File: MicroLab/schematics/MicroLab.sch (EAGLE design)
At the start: 100 parts, among them IC1 MC7805CDTG, IC6 LM324D, J1 POWER_JACKPTH, J2 THONKICONN, J3 THONKICONN, Q901 BC846

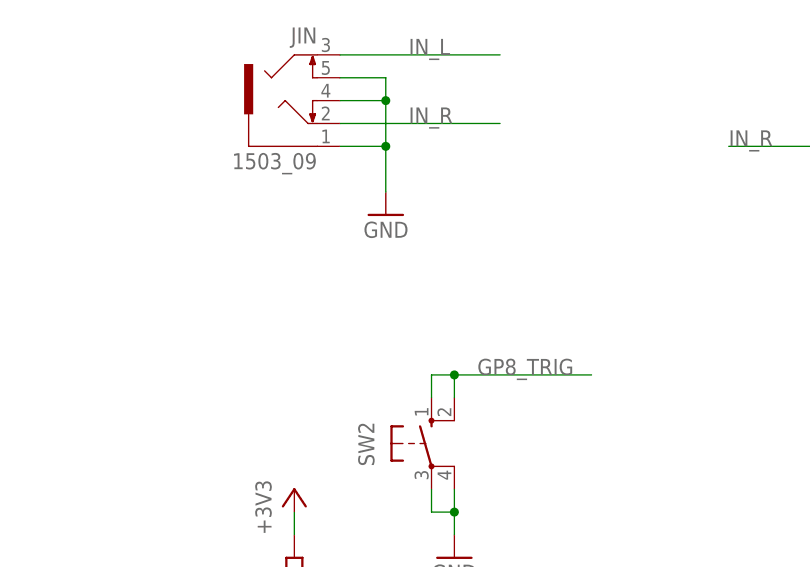
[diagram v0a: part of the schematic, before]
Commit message: added SW3, moved POT_A2
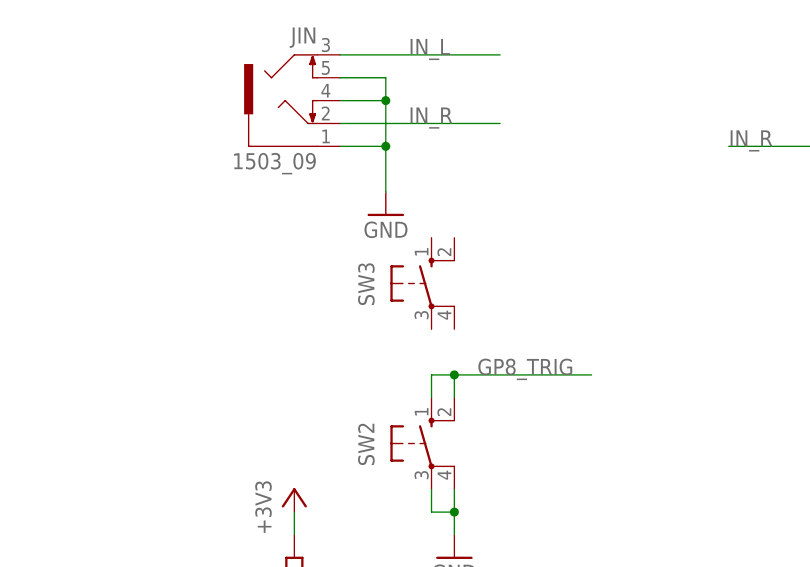
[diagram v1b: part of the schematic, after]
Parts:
- added SW3: (no value), switch-omron:10-XX
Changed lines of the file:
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@@
 <?xml version="1.0" encoding="utf-8"?>
 <!DOCTYPE eagle SYSTEM "eagle.dtd">
-<eagle version="7.5.0">
+<eagle version="7.2.0">
 <drawing>
 <settings>
@@
 <part name="R32" library="Rebel" deviceset="R-EU_" device="0603" value="100R"/>
 <part name="R33" library="Rebel" deviceset="R-EU_" device="0603" value="100R"/>
+<part name="SW3" library="switch-omron" deviceset="10-XX" device=""/>
 </parts>
 <sheets>
@@
 <instance part="R32" gate="G$1" x="231.14" y="157.48" rot="MR180"/>
 <instance part="R33" gate="G$1" x="-53.34" y="48.26" rot="MR180"/>
+<instance part="SW3" gate="1" x="-33.02" y="142.24"/>
 </instances>
 <busses>

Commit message: Completed MicroLab Rev2
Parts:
- removed LED2, LED3, LED4, LED5, LED6, LED7, LED8: KP-3216SGC, SparkFun:LED1206
- removed R15, R23, R24, R25, R27: 1k, Rebel:R-EU_0603
- LED1: value KP-3216SGC -> MULTICOMP_703-1028; device SparkFun:LED1206 -> Rebel:MULTICOMP_703-1028; FARNELL 853-0033 -> (none)
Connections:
- removed net GP9_LEDPWM: R23.1, R25.1, TGP1-4.4
- removed net N$14: LED2.A, R15.2
- removed net N$18: LED7.A, R23.2
- removed net N$20: LED3.A, R24.2
- removed net N$21: LED4.A, R25.2
- removed net N$28: LED5.A, R27.2
- new net GP9_TRIG: SW3.S, SW3.S1, TGP1-4.4
- net +5V: now also LED1.A
- net +9V: now also J1.PWR; no longer J1.GND
- net GND: now also J1.GND, SW3.P, SW3.P1; no longer J1.PWR, LED1.C, LED2.C, LED3.C, LED4.C, LED5.C, LED6.C, LED7.C, LED8.C
- net GP1_LEDPWM: no longer R15.1
- net GP2_LEDPWM: no longer R24.1
- net GP6_LEDPWM: no longer R27.1
- net N$16: now also LED1.CRED; no longer LED1.A
- net N$17: now also LED1.CGREEN; no longer LED6.A
- net N$19: now also LED1.CBLUE; no longer LED8.A
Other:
- moved on the sheet: EXPI, EXPO, J1, J2, JIN, Q901, R21, R22, R28, R33, R34, R36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

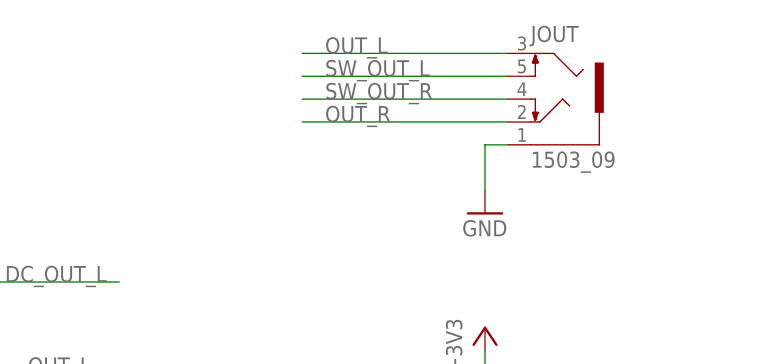
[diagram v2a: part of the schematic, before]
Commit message: removed unused nets from stereo jack
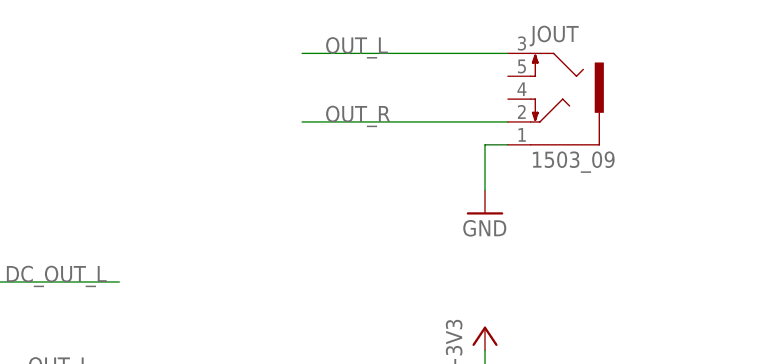
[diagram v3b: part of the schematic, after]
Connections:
- removed net SW_OUT_L: JOUT.5
- removed net SW_OUT_R: JOUT.4
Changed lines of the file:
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@@
-</segment>
-</net>
-<net name="SW_OUT_L" class="0">
-<segment>
-<pinref part="JOUT" gate="G$1" pin="5"/>
-<wire x1="299.72" y1="236.22" x2="276.86" y2="236.22" width="0.1524" layer="91"/>
-<label x="279.4" y="236.22" size="1.778" layer="95"/>
-</segment>
-</net>
-<net name="SW_OUT_R" class="0">
-<segment>
-<pinref part="JOUT" gate="G$1" pin="4"/>
-<wire x1="299.72" y1="233.68" x2="276.86" y2="233.68" width="0.1524" layer="91"/>
-<label x="279.4" y="233.68" size="1.778" layer="95"/>
 </segment>
 </net>

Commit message: MicroLab Rev02
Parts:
- removed POT_A1, POT_A2, POT_A3, POT_A4: POT-ALPS-RK09L1140, Rebel:POT-ALPS-RK09L1140
- added POT_A, POT_B, POT_C, POT_D: POT-ALPS-RK09L1140, Rebel:POT-ALPS-RK09L1140
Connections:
- net +3V3: now also POT_BG$1.3, POT_CG$1.3, POT_DG$1.3; no longer POT_A1G$1.3, POT_A2G$1.3, POT_A4G$1.3
- net ADC1: now also POT_CG$1.2; no longer POT_A1G$1.2
- net ADC2: now also POT_DG$1.2; no longer POT_A2G$1.2
- net ADC3: now also POT_AG$1.2; no longer POT_A3G$1.2
- net ADC4: now also POT_BG$1.2; no longer POT_A4G$1.2
- net GND: now also POT_AG$1.1, POT_AG$2.P$1, POT_BG$1.1, POT_BG$2.P$1, POT_CG$1.1, POT_CG$2.P$1, POT_DG$1.1, POT_DG$2.P$1; no longer POT_A1G$1.1, POT_A1G$2.P$1, POT_A2G$1.1, POT_A2G$2.P$1, POT_A3G$1.1, POT_A3G$2.P$1, POT_A4G$1.1, POT_A4G$2.P$1
- net N$25: now also POT_AG$1.3; no longer POT_A3G$1.3
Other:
- note added: "MicroLab Rev02"
- note removed: "Play Rev01"
- moved on the sheet: D2, J3, JOUT, R29, R30

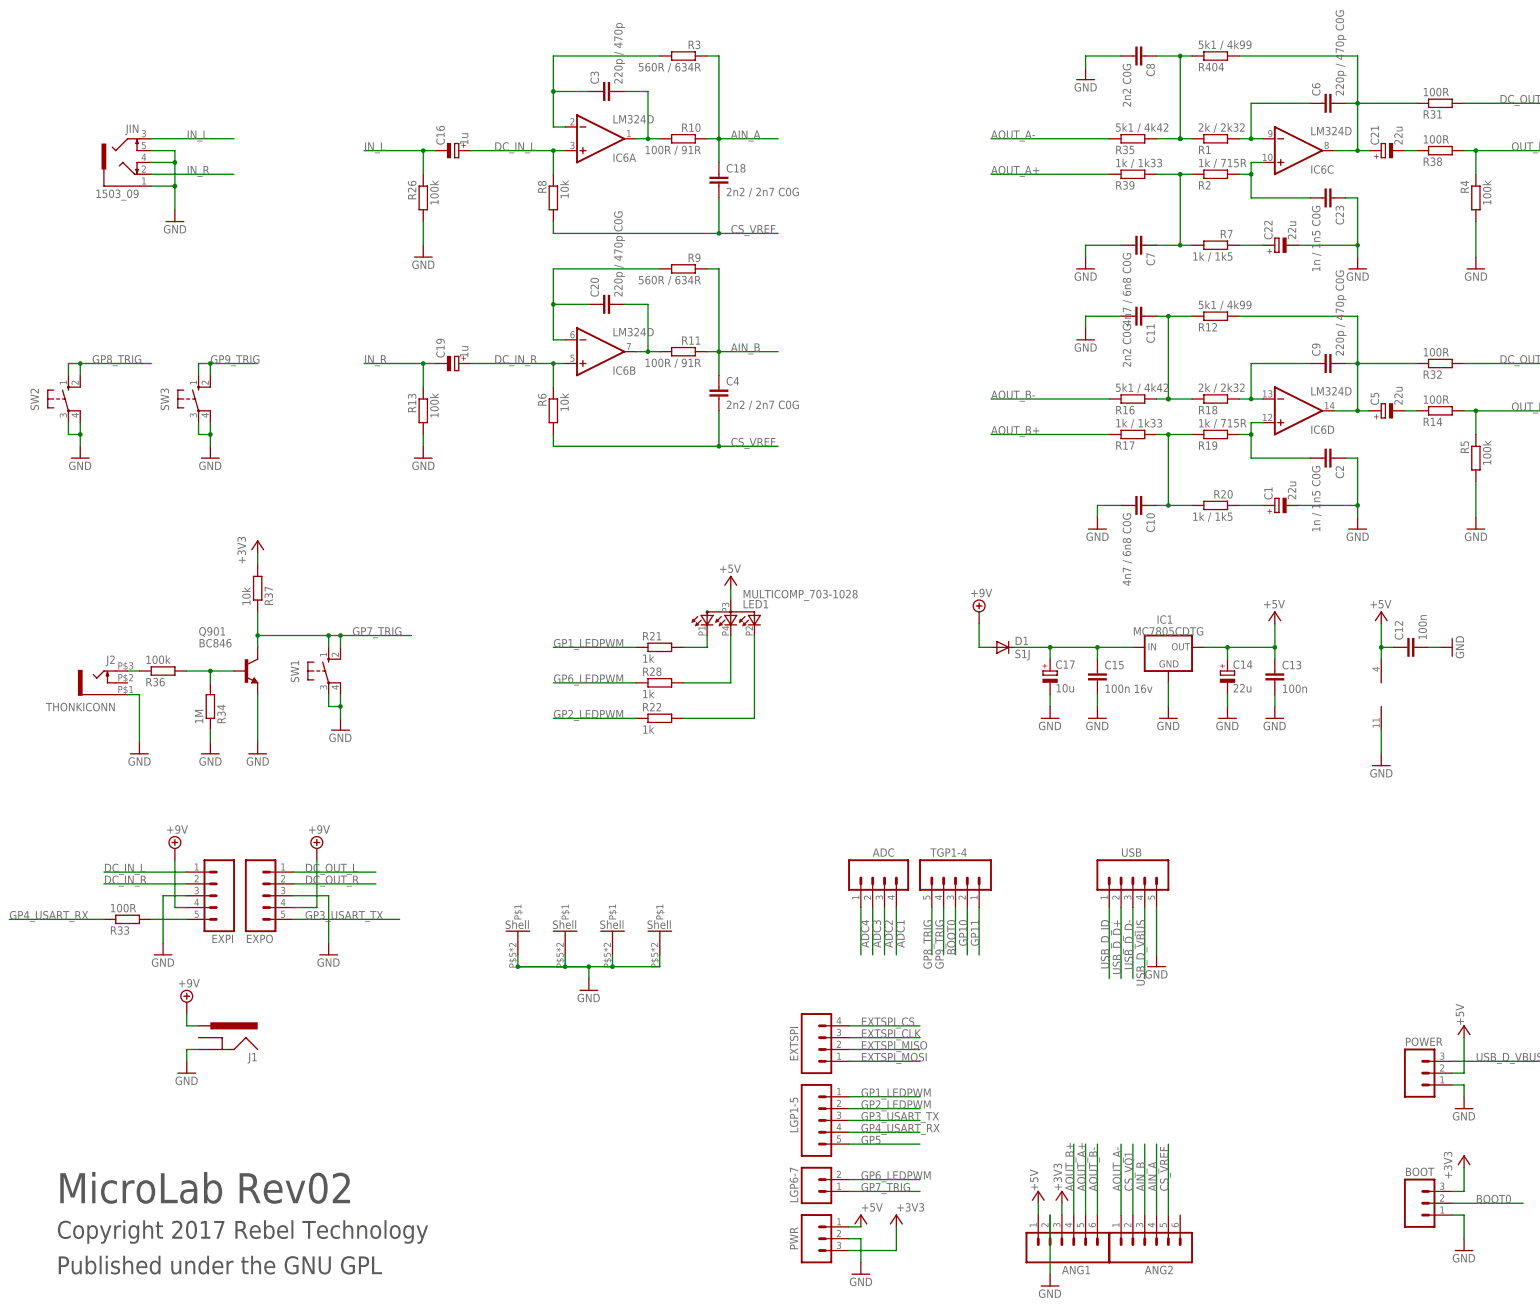
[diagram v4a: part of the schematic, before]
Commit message: changed to JST PH extension headers. Rev03
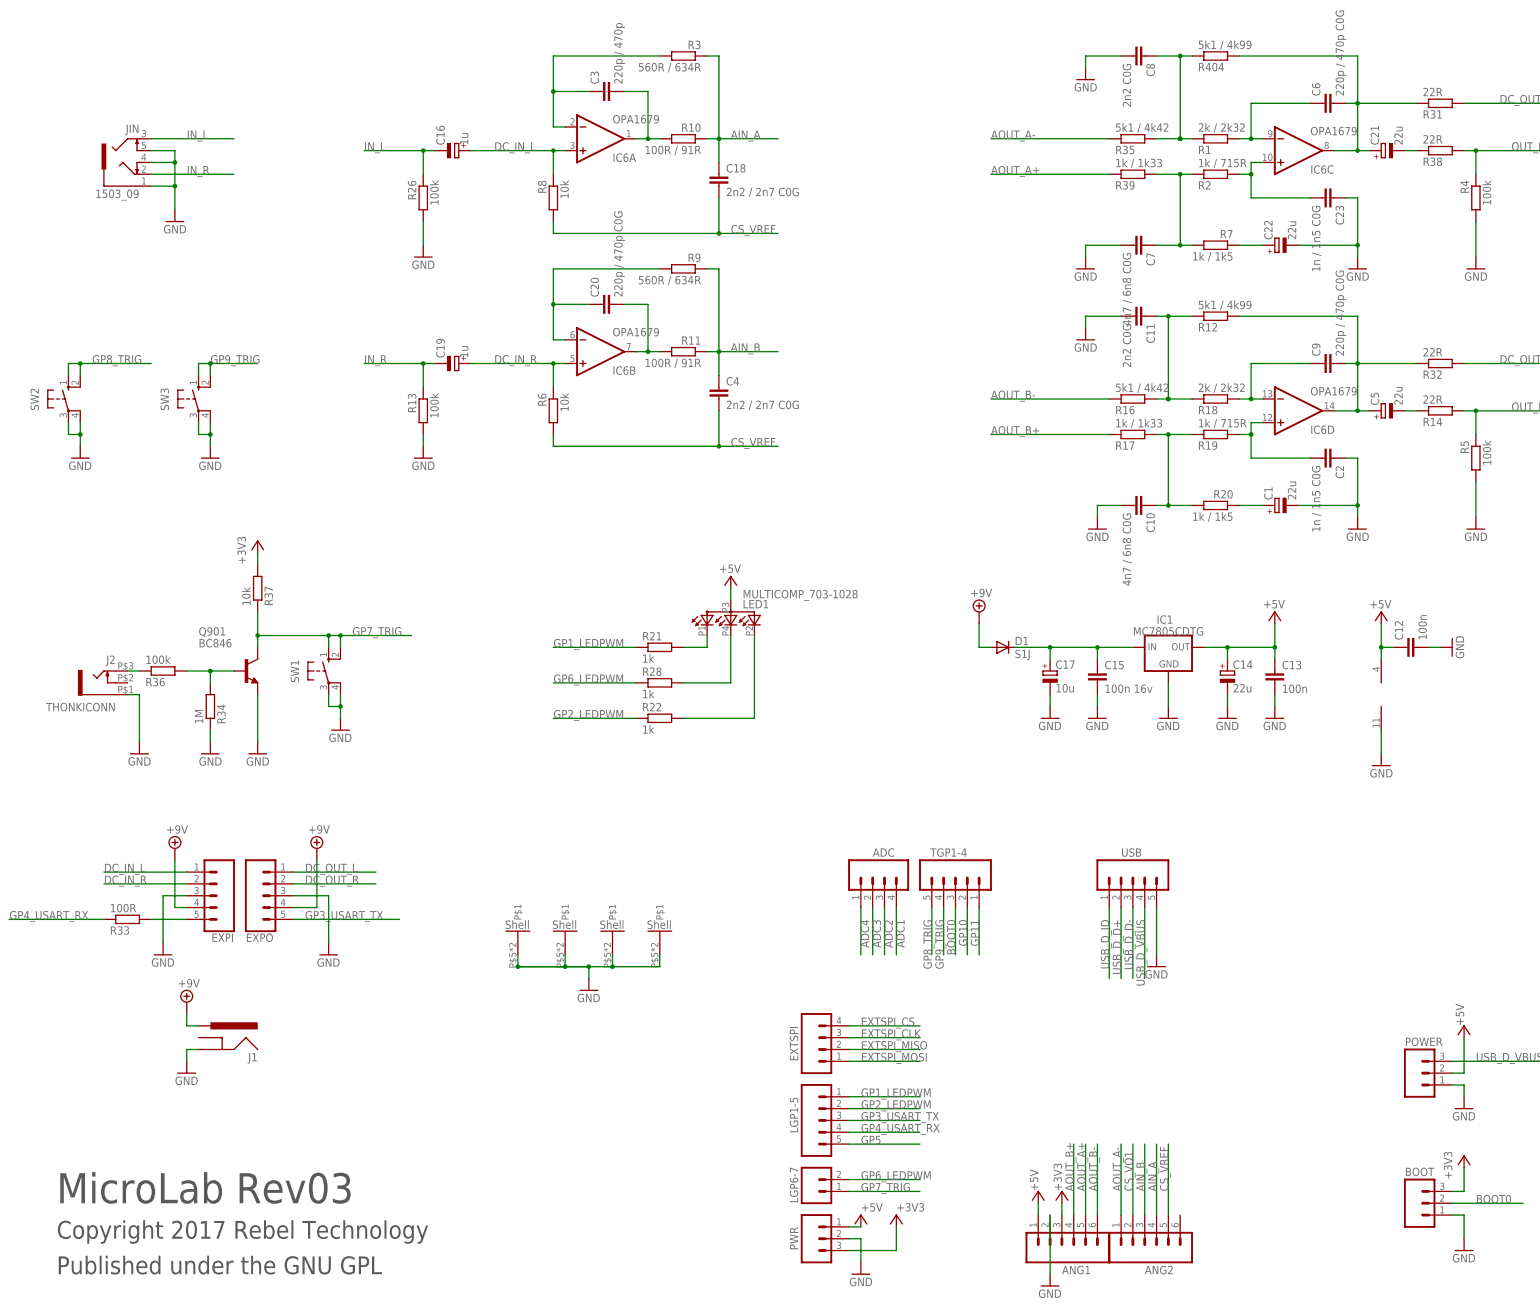
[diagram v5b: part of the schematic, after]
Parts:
- EXPI, EXPO: device SparkFun:M05PTH -> SparkFun-Connectors:CONN_05JST-VERT
- IC6: value LM324D -> OPA1679
- R14, R31, R32, R38: value 100R -> 22R
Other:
- note added: "MicroLab Rev03"
- note removed: "MicroLab Rev02"
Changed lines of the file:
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@@
 <?xml version="1.0" encoding="utf-8"?>
 <!DOCTYPE eagle SYSTEM "eagle.dtd">
-<eagle version="7.5.0">
+<eagle version="8.7.1">
 <drawing>
 <settings>
-<setting alwaysvectorfont="yes"/>
+<setting alwaysvectorfont="no"/>
+<setting keepoldvectorfont="yes"/>
 <setting verticaltext="up"/>
 </settings>
@@
 <layer number="59" name="tCarbon" color="7" fill="1" visible="no" active="no"/>
 <layer number="60" name="bCarbon" color="7" fill="1" visible="no" active="no"/>
+<layer number="88" name="SimResults" color="9" fill="1" visible="no" active="yes"/>
+<layer number="89" name="SimProbes" color="9" fill="1" visible="no" active="yes"/>
 <layer number="90" name="Modules" color="5" fill="1" visible="yes" active="yes"/>
 <layer number="91" name="Nets" color="2" fill="1" visible="yes" active="yes"/>
@@
 <part name="ADC" library="SparkFun" deviceset="M04" device="PTH"/>
 <part name="R404" library="Rebel" deviceset="R-EU_" device="0603" value="5k1 / 4k99"/>
-<part name="R38" library="Rebel" deviceset="R-EU_" device="0603" value="100R"/>
+<part name="R38" library="Rebel" deviceset="R-EU_" device="0603" value="22R"/>
 <part name="R35" library="Rebel" deviceset="R-EU_" device="0603" value="5k1 / 4k42"/>
 <part name="PWR" library="SparkFun" deviceset="M03" device="PTH"/>
@@
 <part name="R7" library="Rebel" deviceset="R-EU_" device="0603" value="1k / 1k5"/>
 <part name="R12" library="Rebel" deviceset="R-EU_" device="0603" value="5k1 / 4k99"/>
-<part name="R14" library="Rebel" deviceset="R-EU_" device="0603" value="100R"/>
+<part name="R14" library="Rebel" deviceset="R-EU_" device="0603" value="22R"/>
 <part name="R16" library="Rebel" deviceset="R-EU_" device="0603" value="5k1 / 4k42"/>
 <part name="R17" library="Rebel" deviceset="R-EU_" device="0603" value="1k / 1k33"/>
@@
 <part name="GND3" library="supply1" deviceset="GND" device=""/>
 <part name="POT_C" library="Rebel" deviceset="POT-ALPS-RK09L" device="1140"/>
-<part name="IC6" library="linear" deviceset="LM324" device="D"/>
+<part name="IC6" library="linear" deviceset="LM324" device="D" value="OPA1679"/>
 <part name="C16" library="Rebel" deviceset="CPOL-EU" device="153CLV-0405" value="1u"/>
 <part name="R26" library="Rebel" deviceset="R-EU_" device="0603" value="100k"/>
@@
 <part name="SW2" library="switch-omron" deviceset="10-XX" device=""/>
 <part name="GND21" library="supply1" deviceset="GND" device=""/>
-<part name="EXPO" library="SparkFun" deviceset="M05" device="PTH"/>
-<part name="EXPI" library="SparkFun" deviceset="M05" device="PTH"/>
+<part name="EXPO" library="SparkFun-Connectors" deviceset="CONN_05" device="JST-VERT"/>
+<part name="EXPI" library="SparkFun-Connectors" deviceset="CONN_05" device="JST-VERT"/>
 <part name="GND22" library="supply1" deviceset="GND" device=""/>
 <part name="GND23" library="supply1" deviceset="GND" device=""/>
@@
 <part name="P+7" library="supply1" deviceset="+5V" device=""/>
 <part name="P+2" library="supply1" deviceset="+5V" device=""/>
-<part name="R31" library="Rebel" deviceset="R-EU_" device="0603" value="100R"/>
-<part name="R32" library="Rebel" deviceset="R-EU_" device="0603" value="100R"/>
+<part name="R31" library="Rebel" deviceset="R-EU_" device="0603" value="22R"/>
+<part name="R32" library="Rebel" deviceset="R-EU_" device="0603" value="22R"/>
 <part name="R33" library="Rebel" deviceset="R-EU_" device="0603" value="100R"/>
 <part name="SW3" library="switch-omron" deviceset="10-XX" device=""/>
@@
 <sheet>
 <plain>
-<text x="-66.04" y="-22.86" size="6.4516" layer="97" font="vector">MicroLab Rev02</text>
+<text x="-66.04" y="-22.86" size="6.4516" layer="97" font="vector">MicroLab Rev03</text>
 <text x="-66.04" y="-30.48" size="3.81" layer="97" font="vector">Copyright 2017 Rebel Technology</text>
 <text x="-66.04" y="-38.1" size="3.81" layer="97" font="vector">Published under the GNU GPL</text>
